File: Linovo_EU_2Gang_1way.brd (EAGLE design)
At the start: 43 x 43 mm, 41 parts, among them IC1 ATMEGA328P, U1 ATSHA204A, U2 RFM69_MINIMAL

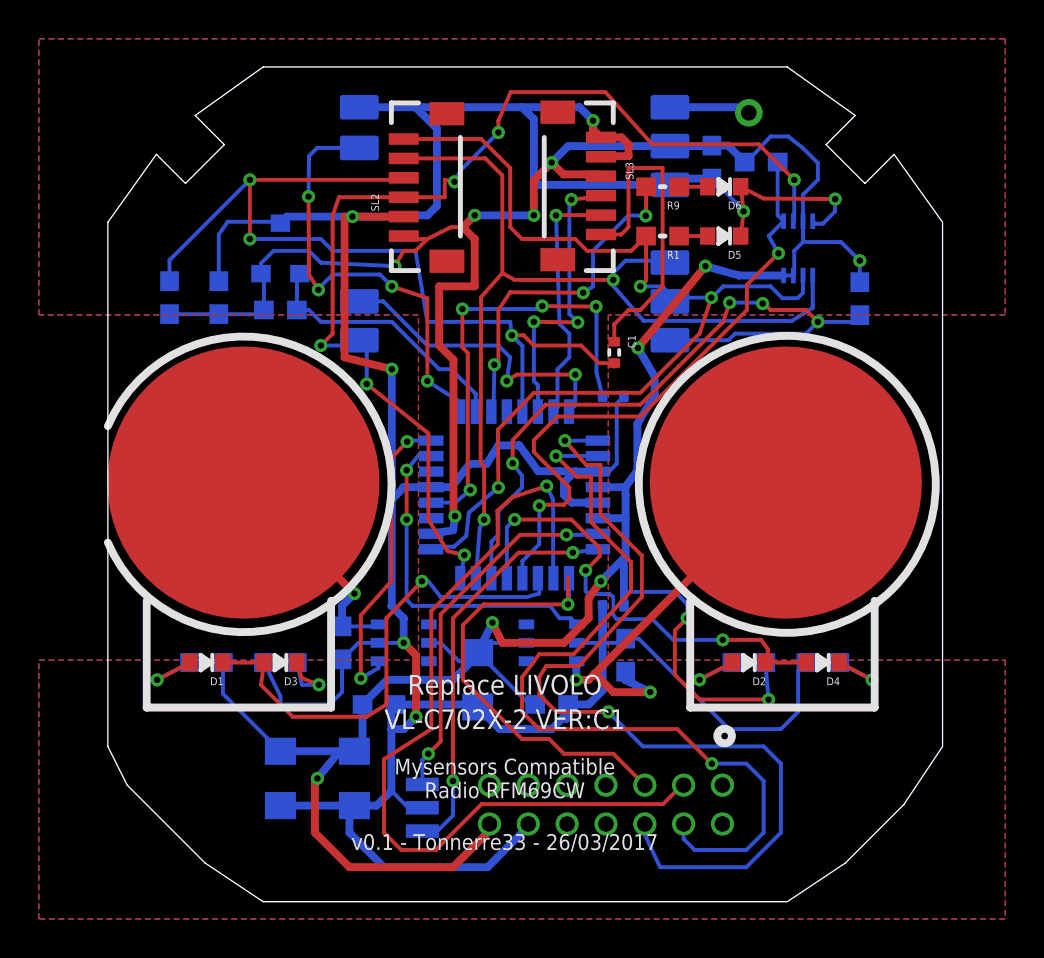
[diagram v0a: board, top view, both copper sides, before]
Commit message: replace senspad & reroot
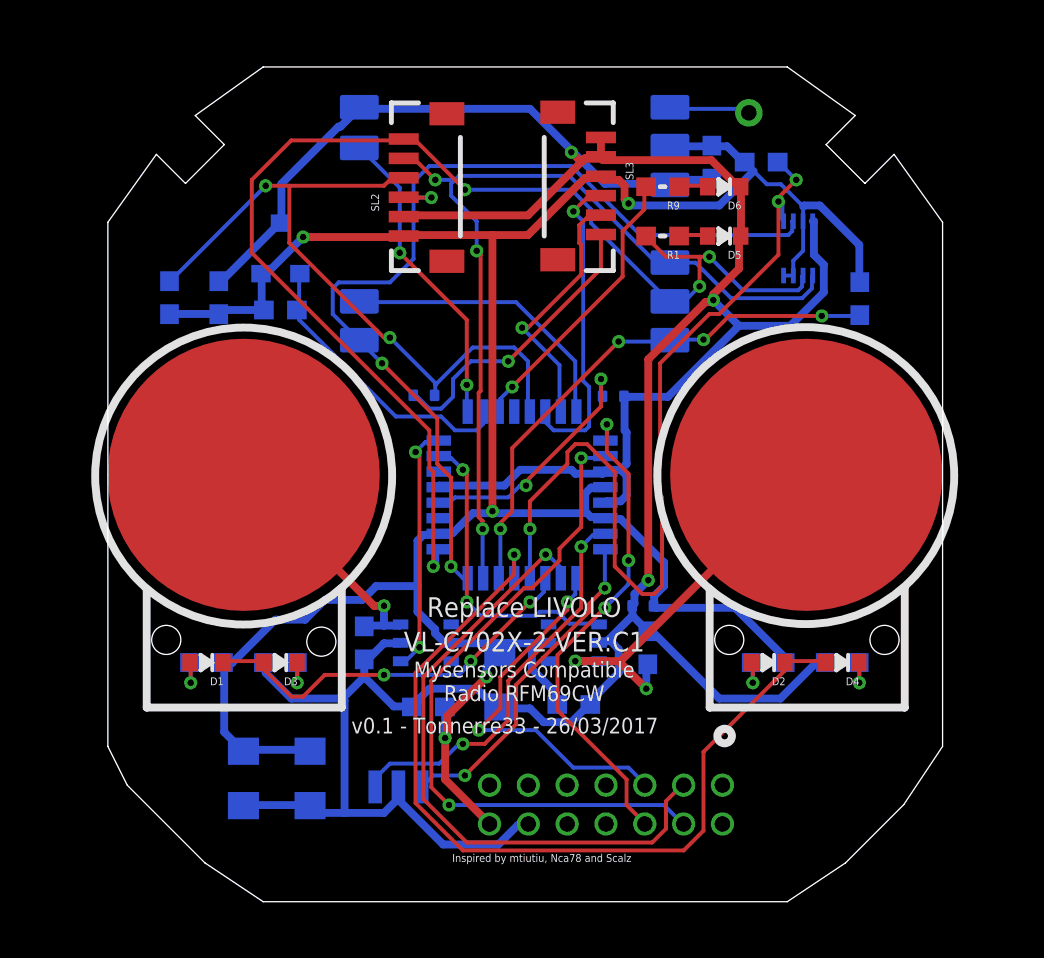
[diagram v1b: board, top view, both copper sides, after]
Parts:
- moved C1 10.1 mm to (16.3, 26.1), flipped to the bottom, turned to 180 degrees
- moved C9 2.54 mm to (16.5, 10.0), turned to 180 degrees
- moved C11 2.29 mm to (10.4, 6.35)
- moved C10 1.91 mm to (6.99, 6.35)
- moved U$3 1.63 mm to (15.0, 5.91), turned to 180 degrees
- moved C6 1.52 mm to (27.6, 15.2)
- moved C4 1.20 mm to (27.8, 13.1)
- moved C12 1.14 mm to (20.2, 11.4)
- moved C7 1.14 mm to (24.0, 10.2)
- moved C8 1.14 mm to (13.2, 13.3)
- moved U$4 1.14 mm to (25.3, 15.2)
- moved U$6 1.14 mm to (15.1, 11.4)
- moved U$1 1.12 mm to (36.0, 22.0)
- moved D2 1.00 mm to (34.0, 12.3)
- moved D4 1.00 mm to (37.8, 12.3)
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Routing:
- net VCC: track 173.3 -> 143.8 mm, vias 13 -> 5
- net L1_SET: track 46.7 -> 25.3 mm, vias 2 -> 3
- net LED2: track 24.7 -> 45.0 mm, vias 3 -> 1
- net FLASH_CS: track 32.2 -> 45.2 mm, vias 2 -> 3
- net SCK: track 52.7 -> 64.4 mm, vias 3 -> 4
- net L2_SET: track 44.3 -> 33.2 mm
- net N$4: track 23.5 -> 12.9 mm, vias 4 -> 2
- net CSN: track 37.7 -> 27.8 mm
- net RST: track 45.7 -> 36.9 mm, vias 3 -> 2
- net GND: track 187.2 -> 179.2 mm, vias 7 -> 3
- net L1_RST: track 42.7 -> 35.5 mm
- net A2: track 22.9 -> 15.9 mm, vias 4 -> 2
- net MISO: track 56.8 -> 51.0 mm, vias 6 -> 3
- net L2_RST: track 24.4 -> 19.7 mm, vias 1 -> 2
- net LED1: track 25.0 -> 20.7 mm, vias 1 -> 3
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- removed copper zone on layer 1, net GND
- removed copper zone on layer 16, net GND
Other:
- board text added: "Inspired by mtiutiu, Nca78 and Scalz"

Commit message: Change value RFM69 capacitor
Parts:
- C3: value 4u7 -> 10u
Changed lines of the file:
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@@
 <element name="C1" library="LowPowerLab" package="0402-CAP" value="100n" x="16.2814" y="26.0858" rot="MR180"/>
 <element name="C2" library="LowPowerLab" package="0402-CAP" value="100n" x="26.035" y="26.035" rot="MR0"/>
-<element name="C3" library="LowPowerLab" package="0603-CAP" value="4u7" x="31.115" y="38.1" rot="MR270"/>
+<element name="C3" library="LowPowerLab" package="0603-CAP" value="10u" x="31.115" y="38.1" rot="MR270"/>
 <element name="D5" library="LowPowerLab" package="0603-LED" value="LED0603" x="31.75" y="34.29" rot="R180"/>
 <element name="IC1" library="LowPowerLab" package="TQFP32-08" value="ATMEGA328P" x="21.336" y="20.955" rot="MR0"/>
